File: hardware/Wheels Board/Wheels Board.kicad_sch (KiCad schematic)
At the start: 0 parts

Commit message: Wheels Board Rev A (#3)
* current rev a

* schematic v1

* Rev a final draft

* footprints

* +op amp, breakout, footprints

* switched to pads for hall sensor wires

* layout planning

* added uart to sch

* concepts of revA layout

* review council changes, layout not finalized

* pre wiring layout

* revised layout again

* revised layout

* new board dimensions

* final revisions!

i didnt do pn yet

* pre-2.4mm connector experiment

(will jump back to this if all goes wrong)

* pls pls pls

* pls pls pls

* final rev a labels added

* silkscreen changes

* Resolved DRC errors

* generated bom

* added hall effect sensor PN

* bom csv

---------

Co-authored-by: Frank Li <fxl77@my.utexas.edu>
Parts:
- added C1, C2, C4: 100nf, Capacitor_SMD:C_0603_1608Metric_Pad1.08x0.95mm_HandSolder, symbol Device:C
- added C3: 10uf, Capacitor_SMD:C_0603_1608Metric_Pad1.08x0.95mm_HandSolder, symbol Device:C
- added D2, D3, D4, D5: LED, LED_SMD:LED_0603_1608Metric_Pad1.05x0.95mm_HandSolder, symbol Device:LED
- added D7: MBR0520LT1G, diode:SOD3716X135N, symbol MBR0520LT1G (diode):MBR0520LT1G
- added F1: Fuse, Fuse:FUSE_3568, symbol Device:Fuse
- added J1, J2: Conn_01x05, Connector_PinHeader_2.54mm:PinHeader_1x05_P2.54mm_Vertical, symbol Connector_Generic:Conn_01x05
- added J3: Conn_01x03, Connector_PinHeader_2.54mm:PinHeader_1x03_P2.54mm_Vertical, symbol Connector_Generic:Conn_01x03
- added J4: 53307-2471, UTSVT_Connectors:PeripheralSOM, symbol utsvt_connectors:PeripheralSOMConnector
- added J5: MX150_02x02_Vertical, UTSVT_Connectors:MX150_02x02_Vertical, symbol utsvt_connectors:MX150_02x02_Vertical
- added LOGO1: LHRS, UTSVT_Logos:LHRs_LOGO, symbol utsvt_misc:Logo_Placeholder
- added LOGO2: Rooster, UTSVT_Logos:roosters, symbol utsvt_misc:Logo_Placeholder
- added LOGO3: HALL EFFECT SENSOR, symbol utsvt_misc:Logo_Placeholder
- added R1, R3, R4: 1.5k, Resistor_SMD:R_0603_1608Metric_Pad0.98x0.95mm_HandSolder, symbol Device:R
- added R2: 4.2k, Resistor_SMD:R_0603_1608Metric_Pad0.98x0.95mm_HandSolder, symbol Device:R
- added R7, R8: 10k, Resistor_SMD:R_0603_1608Metric_Pad0.98x0.95mm_HandSolder, symbol Device:R
- added TP_3.1, TP_3.2, TP_3.3, TP_3.4, TP_5V1, TP_GND1: TestPoint, TestPoint:TestPoint_Pad_1.0x1.0mm, symbol Connector:TestPoint
- added U1: ASM330LHHTR, ASM330LHHTR-IMU:LGA-14L_2P5X3X0P83_STM, symbol AIMU-SM330LHHTR:ASM330LHHTR
- added U2: XIAO-ESP32-S3-SMD, XIAO-ESP32S3:XIAO-ESP32S3-DIP, symbol xiao-esp32s3-smd:XIAO-ESP32-S3-SMD
- added U3: TLV9001IDCK, Package_TO_SOT_SMD:SOT-353_SC-70-5, symbol Amplifier_Operational:TLV9001IDCK
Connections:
- new net: C2.1, F1.2, J3.3 (Pin_3)
- new net: D4.1 (K), R3.1
- new net: D7.C, U2.14 (5V)
- new net: D3.1 (K), R2.1
- new net: D5.1 (K), R4.1
- new net: D2.1 (K), R1.1
- new net +24V: D3.2 (A), J4.24 (+24V_In), J5.1 (+24V), TP_3.4.1
- new net +3.3V: C1.1, C3.1, C4.1, D4.2 (A), J4.2 (+3.3v), TP_3.1.1, U1.5 (VDD_IO), U1.8 (VDD), U3.5 (V+)
- new net +5V: D2.2 (A), D7.A, F1.1, TP_5V1.1
- new net CAN_+: J4.22 (CAN_H), J5.2 (CANH_IN)
- new net CAN_-: J4.20 (CAN_L), J5.4 (CANH_OUT)
- new net ESP_SPI_CLK: J1.4 (Pin_4), J4.18 (SPI2_SCK), U2.9 (GPIO7_A8_D8_SCK)
- new net ESP_SPI_MISO: J1.2 (Pin_2), J4.14 (SPI2_MISO), U2.10 (GPIO8_A9_D9_MISO)
- new net ESP_SPI_MOSI: J1.3 (Pin_3), J4.16 (SPI2_MOSI), U2.11 (GPIO9_A10_D10_MOSI)
- new net ESP_SPI_SS: J1.1 (Pin_1), J4.12 (SPI2_NSS), U2.4 (GPIO4_A3_D3)
- new net ESP_UART_RX: J4.4 (I2C1_SDA), U2.8 (GPIO44_D7_RX)
- new net ESP_UART_TX: J4.6 (I2C1_SCL), U2.7 (GPIO43_A6_D6_TX)
- new net EXTRA_GPIO1: J4.7 (OPAMP1_VINP), U2.2 (GPIO2_A1_D1)
- new net EXTRA_GPIO2: J4.9 (ADC1_IN7), U2.3 (GPIO3_A2_D2)
- new net GND: C1.2, C2.2, C3.2, C4.2, J1.5 (Pin_5), J2.5 (Pin_5), J3.1 (Pin_1), J4.1 (GND), J4.3 (GND), J4.5 (GND), J5.3 (GND), R1.2, R2.2, R3.2, R4.2, R7.2, R8.2, TP_GND1.1, U1.2 (RES), U1.3 (RES), U1.6 (GND), U1.7 (GND), U2.13 (GND), U2.16 (GND), U2.20 (GND), U2.25 (PAD), U3.2 (V-)
- new net HALL_FEEDBACK: J4.11 (ADC1_IN9), U3.3 (-), U3.4
- new net HALL_OUT: J3.2 (Pin_2), U3.1 (+)
- new net IMU_INT1: J4.13 (ADC1_IN10), R8.1, TP_3.2.1, U1.4 (INT1)
- new net IMU_INT2: J4.15 (ADC1_IN11), R7.1, TP_3.3.1, U1.9 (INT2)
- new net IMU_SPI_CLK: J2.1 (Pin_1), J4.23 (SPI1_SCK), U1.13 (SCL)
- new net IMU_SPI_MISO: J2.2 (Pin_2), J4.21 (SPI1_MISO), U1.1 (SDO/SA0)
- new net IMU_SPI_MOSI: J2.4 (Pin_4), J4.17 (SPI1_MOSI), U1.14 (SDA)
- new net IMU_SPI_SS: J2.3 (Pin_3), J4.19 (SPI1_NSS), U1.12 (CS)
- new net XIAO_HEARTBEAT_LED: D5.2 (A), U2.1 (GPIO1_A0_D0)
- no-connect marks 0 -> 13
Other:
- added sheet 24v to 5v convertor (Voltage_Convertor.kicad_sch)
- note added: "6-AXIS IMU"
- note added: "LEDS"
- note added: "LHR GRAPHICS"
- note added: "MX150_CONNECTOR"
- note added: "PSOM CONNECTIONS"
- note added: "Pads for hall effect sensor: 934-555050002A"
- note added: "TESTING"
- note added: "UNITYGAIN OP AMP"
- note added: "XIAO ESP32S3 MC"
- note added: "using adc as gpio"
- title: (none) -> Wheels Sensor Board

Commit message: Left rev b layout
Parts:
- removed J2: Conn_01x05, Connector_PinHeader_2.54mm:PinHeader_1x05_P2.54mm_Vertical, symbol Connector_Generic:Conn_01x05
- removed J5: MX150_02x02_Vertical, UTSVT_Connectors:MX150_02x02_Vertical, symbol utsvt_connectors:MX150_02x02_Vertical
- removed TP_3.2, TP_3.3: TestPoint, TestPoint:TestPoint_Pad_1.0x1.0mm, symbol Connector:TestPoint
- added J5: Conn_01x02, Connector_PinHeader_2.54mm:PinHeader_1x02_P2.54mm_Vertical, symbol Connector_Generic:Conn_01x02
- added J6: Conn_01x05_Pin, Connector_Molex:Molex_Nano-Fit_105313-xx04_1x04_P2.50mm_Horizontal, symbol Connector:Conn_01x05_Pin
- added J7: Conn_01x07, Connector_PinHeader_2.54mm:PinHeader_1x07_P2.54mm_Vertical, symbol Connector_Generic:Conn_01x07
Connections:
- net +24V: now also J6.1 (Pin_1)
- net +3.3V: now also J5.1 (Pin_1)
- net CAN_+: now also J6.2 (Pin_2)
- net CAN_-: now also J6.4 (Pin_4)
- net ESP_SPI_CLK: now also J1.2 (Pin_2); no longer J1.4 (Pin_4)
- net ESP_SPI_MISO: now also J1.3 (Pin_3); no longer J1.2 (Pin_2)
- net ESP_SPI_MOSI: now also J1.4 (Pin_4); no longer J1.3 (Pin_3)
- net GND: now also J5.2 (Pin_2), J6.3 (Pin_3), J6.5 (Pin_5), J7.1 (Pin_1)
- net IMU_INT1: now also J7.2 (Pin_2)
- net IMU_INT2: now also J7.3 (Pin_3)
- net IMU_SPI_CLK: now also J7.6 (Pin_6)
- net IMU_SPI_MISO: now also J7.4 (Pin_4)
- net IMU_SPI_MOSI: now also J7.5 (Pin_5)
- net IMU_SPI_SS: now also J7.7 (Pin_7)
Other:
- note added: "nano-fit conn"
- note removed: "MX150_CONNECTOR"
- moved on the sheet: J1, TP_3.1, TP_5V1, TP_GND1

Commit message: ignore invert file for now
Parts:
- removed TP_3.1, TP_3.4, TP_5V1, TP_GND1: TestPoint, TestPoint:TestPoint_Pad_1.0x1.0mm, symbol Connector:TestPoint
- removed U3: TLV9001IDCK, Package_TO_SOT_SMD:SOT-353_SC-70-5, symbol Amplifier_Operational:TLV9001IDCK
- added J10: gnd, Connector_PinHeader_2.54mm:PinHeader_1x01_P2.54mm_Vertical, symbol Connector:Conn_01x01_Socket
- added J11: hall_out, Connector_PinHeader_2.54mm:PinHeader_1x01_P2.54mm_Vertical, symbol Connector:Conn_01x01_Socket
- added J2: 24v, Connector_PinHeader_2.54mm:PinHeader_1x01_P2.54mm_Vertical, symbol Connector:Conn_01x01_Socket
- added J8: Conn_01x03, Connector_PinHeader_2.54mm:PinHeader_1x03_P2.54mm_Vertical, symbol Connector_Generic:Conn_01x03
- added J9: 5v, Connector_PinHeader_2.54mm:PinHeader_1x01_P2.54mm_Vertical, symbol Connector:Conn_01x01_Socket
- added U5: TLV9002QDRQ1, Package_SO:SOIC-8_3.9x4.9mm_P1.27mm, symbol utsvt_misc:TLV9002QDRQ1
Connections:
- net +24V: now also J2.1 (Pin_1)
- net +3.3V: now also U5.8 (V+)
- net +5V: now also J9.1 (Pin_1)
- net ESP_UART_RX: now also J8.1 (Pin_1)
- net ESP_UART_TX: now also J8.2 (Pin_2)
- net GND: now also J10.1 (Pin_1), J8.3 (Pin_3), U5.4 (V-)
- net HALL_OUT: now also J11.1 (Pin_1), U5.3 (+)
- net CAN_+ renamed CAN_H
- net CAN_- renamed CAN_L
- net HALL_FEEDBACK renamed HALL_PSOM
- net HALL_PSOM: now also U5.1, U5.2 (-)
- no-connect marks 13 -> 16
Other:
- moved on the sheet: J5

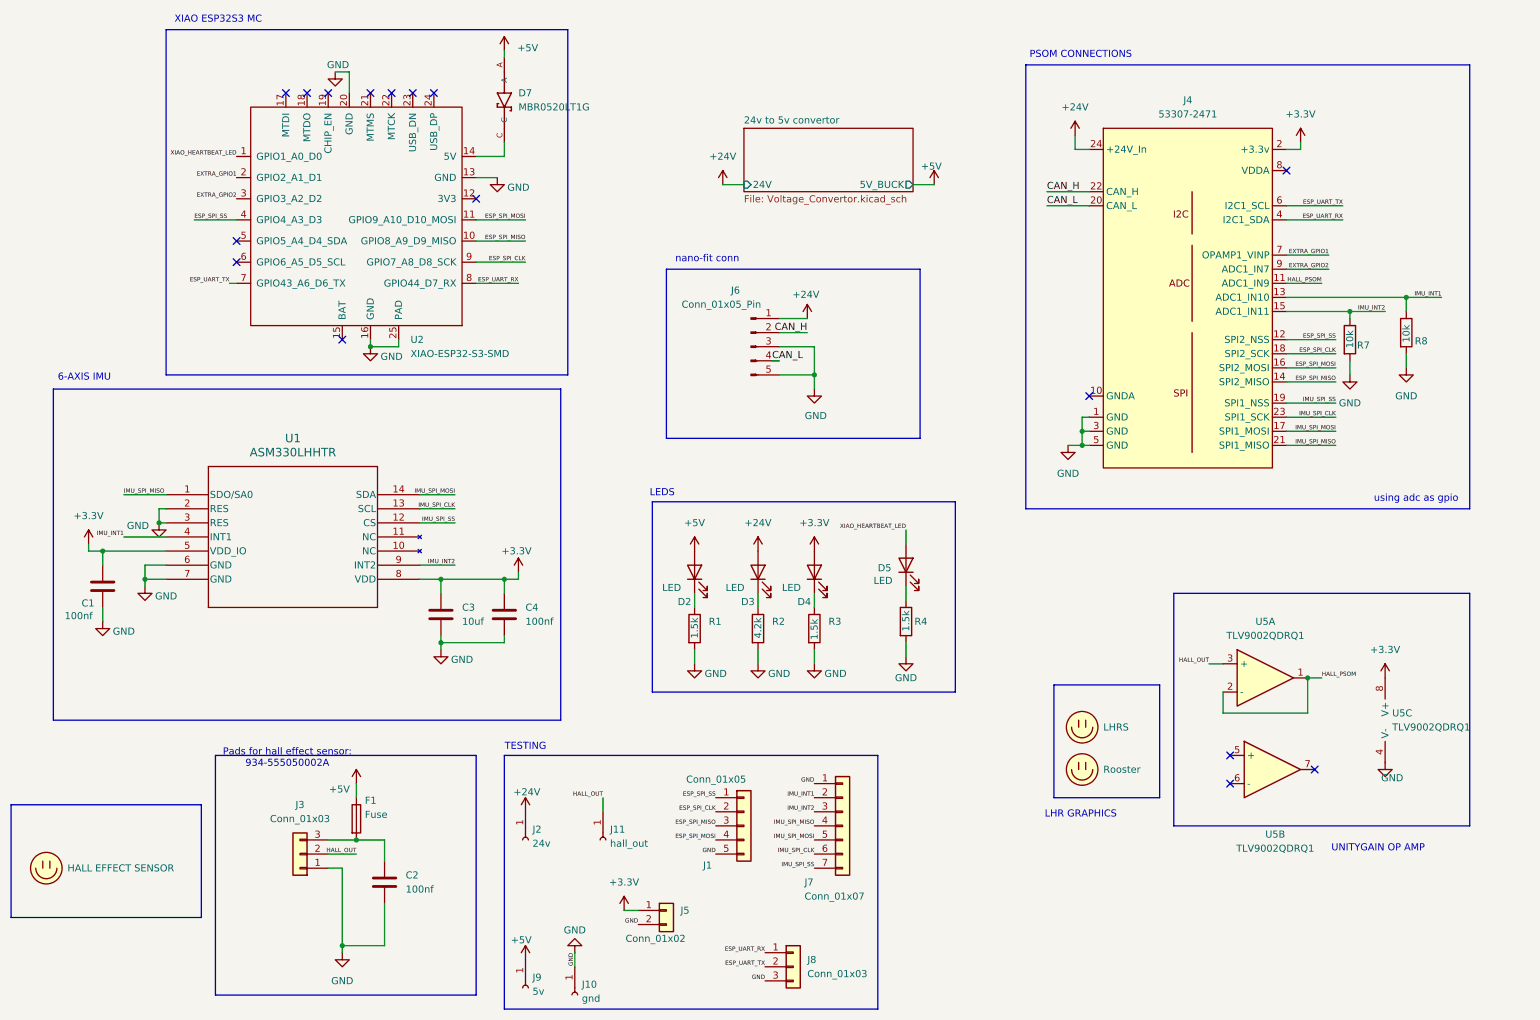
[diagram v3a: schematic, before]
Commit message: conn changes
rotated can conn, changed hall conn to hor, fixed tp clearance
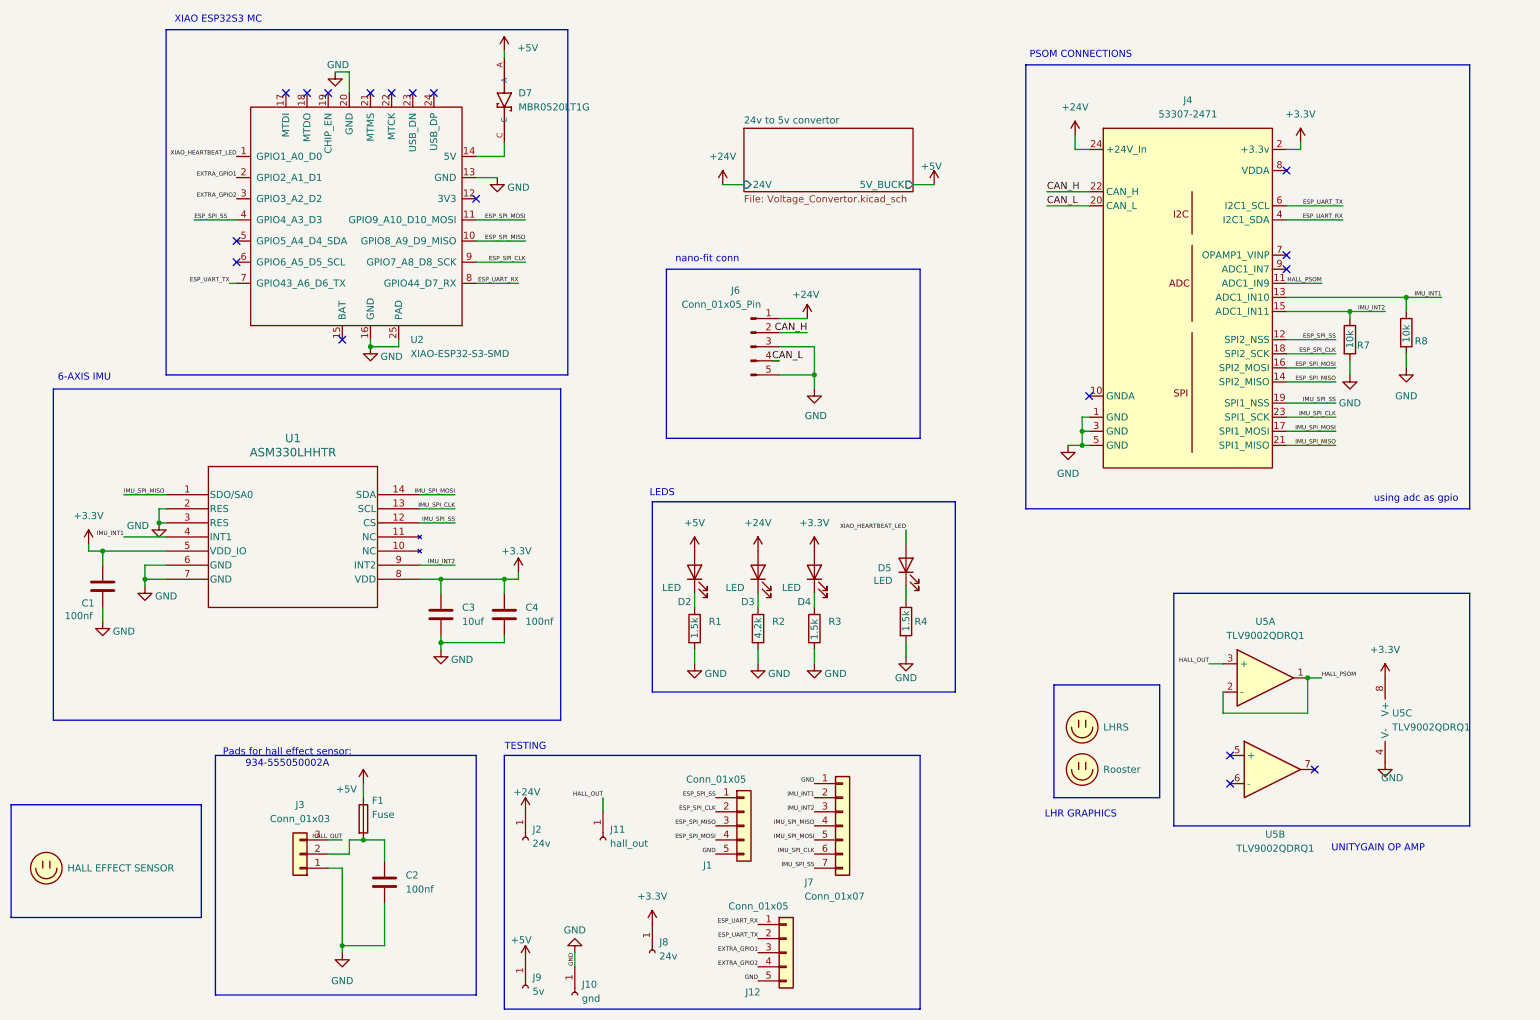
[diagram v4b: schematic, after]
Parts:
- removed J5: Conn_01x02, Connector_PinHeader_2.54mm:PinHeader_1x02_P2.54mm_Vertical, symbol Connector_Generic:Conn_01x02
- removed J8: Conn_01x03, Connector_PinHeader_2.54mm:PinHeader_1x03_P2.54mm_Vertical, symbol Connector_Generic:Conn_01x03
- added J12: Conn_01x05, Connector_PinHeader_2.54mm:PinHeader_1x05_P2.54mm_Vertical, symbol Connector_Generic:Conn_01x05
- added J8: 24v, Connector_PinHeader_2.54mm:PinHeader_1x01_P2.54mm_Vertical, symbol Connector:Conn_01x01_Socket
- J3: footprint Connector_PinHeader_2.54mm:PinHeader_1x03_P2.54mm_Vertical -> Connector_PinHeader_2.54mm:PinHeader_1x03_P2.54mm_Horizontal
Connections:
- net +3.3V: now also J8.1 (Pin_1)
- net ESP_UART_RX: now also J12.1 (Pin_1)
- net ESP_UART_TX: now also J12.2 (Pin_2)
- net EXTRA_GPIO1: now also J12.3 (Pin_3); no longer J4.7 (OPAMP1_VINP)
- net EXTRA_GPIO2: now also J12.4 (Pin_4); no longer J4.9 (ADC1_IN7)
- net GND: now also J12.5 (Pin_5)
- net HALL_OUT: now also J3.3 (Pin_3); no longer J3.2 (Pin_2)
- net at C2.1, F1.2: now also J3.2 (Pin_2); no longer J3.3 (Pin_3)
- no-connect marks 16 -> 18
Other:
- moved on the sheet: F1

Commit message: lcsc
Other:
- moved on the sheet: J10, J8, J9

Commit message: added bypass cap to hall
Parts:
- added C13: 1uf, Capacitor_SMD:C_0603_1608Metric_Pad1.08x0.95mm_HandSolder, symbol Device:C
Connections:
- net +3.3V: now also C13.1
- net GND: now also C13.2
